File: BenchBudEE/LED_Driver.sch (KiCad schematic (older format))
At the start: 0 parts

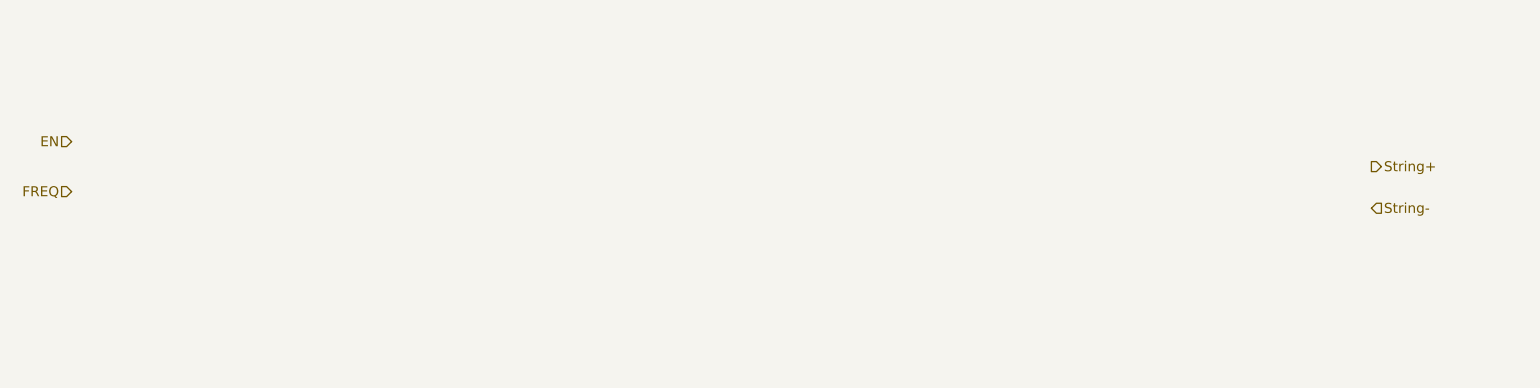
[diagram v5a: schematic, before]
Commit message: LED Driver module sketched out from AP5726 chip
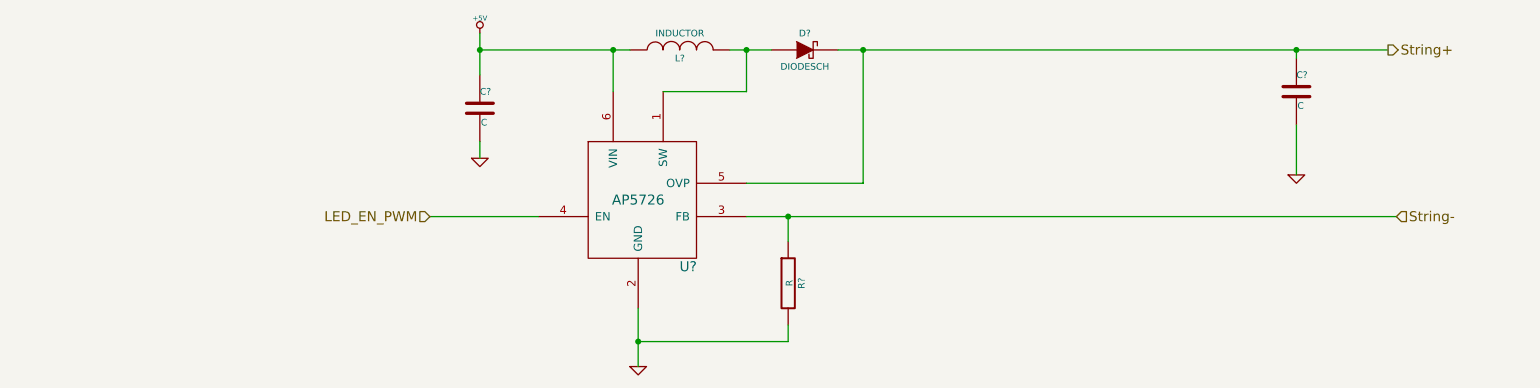
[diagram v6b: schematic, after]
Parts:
- added C? (x2): C, ~, symbol C
- added D?: DIODESCH, ~, symbol DIODESCH
- added L?: INDUCTOR, ~, symbol INDUCTOR
- added R?: R, ~, symbol R
- added U?: AP5726, symbol AP5726
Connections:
- net String+: now also C?.1, D?.2 (K), U?.5 (OVP)
- net String-: now also R?.1, U?.3 (FB)
- new net: D?.1 (A), L?.2, U?.1 (SW)
- new net +5V: C?.1, L?.1, U?.6 (VIN)
- new net GND: C?.2, C?.2, R?.2, U?.2 (GND)
- new net LED_EN_PWM: U?.4 (EN)
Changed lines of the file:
@@
 Comment4 ""
 $EndDescr
-Text HLabel 1600 2500 0    60   Input ~ 0
-EN
-Text HLabel 1600 2800 0    60   Input ~ 0
-FREQ
-Text HLabel 9400 2650 2    60   Output ~ 0
+Text HLabel 3750 2950 0    60   Input ~ 0
+LED_EN_PWM
+Text HLabel 9500 1950 2    60   Output ~ 0
 String+
-Text HLabel 9400 2900 2    60   Input ~ 0
+Text HLabel 9550 2950 2    60   Input ~ 0
 String-
+$Comp
+L AP5726 U?
+U 1 1 52F3F91E
+P 5000 2850
+F 0 "U?" H 5300 2450 60  0000 C CNN
+F 1 "AP5726" H 5000 2850 60  0000 C CNN
+F 2 "" H 4950 2900 60  0000 C CNN
+F 3 "" H 4950 2900 60  0000 C CNN
+	1    5000 2850
+	1    0    0    -1
+$EndComp
+$Comp
+L +5V #PWR?
+U 1 1 52F3FC4A
+P 4050 1850
+F 0 "#PWR?" H 4050 1940 20  0001 C CNN
+F 1 "+5V" H 4050 1940 30  0000 C CNN
+F 2 "" H 4050 1850 60  0000 C CNN
+F 3 "" H 4050 1850 60  0000 C CNN
+	1    4050 1850
+	1    0    0    -1
+$EndComp
+$Comp
+L GND #PWR?
+U 1 1 52F3FC59
+P 5000 3850
+F 0 "#PWR?" H 5000 3850 30  0001 C CNN
+F 1 "GND" H 5000 3780 30  0001 C CNN
+F 2 "" H 5000 3850 60  0000 C CNN
+F 3 "" H 5000 3850 60  0000 C CNN
+	1    5000 3850
+	1    0    0    -1
+$EndComp
+Wire Wire Line
+	5000 3500 5000 3850
+$Comp
+L GND #PWR?
+U 1 1 52F3FC67
+P 4050 2600
+F 0 "#PWR?" H 4050 2600 30  0001 C CNN
+F 1 "GND" H 4050 2530 30  0001 C CNN
+F 2 "" H 4050 2600 60  0000 C CNN
+F 3 "" H 4050 2600 60  0000 C CNN
+	1    4050 2600
+	1    0    0    -1
+$EndComp
+$Comp
+L C C?
+U 1 1 52F3FC6F
+P 4050 2300
+F 0 "C?" H 4050 2400 40  0000 L CNN
+F 1 "C" H 4056 2215 40  0000 L CNN
+F 2 "~" H 4088 2150 30  0000 C CNN
+F 3 "~" H 4050 2300 60  0000 C CNN
+	1    4050 2300
+	1    0    0    -1
+$EndComp
+Wire Wire Line
+	4050 1850 4050 2100
+Wire Wire Line
+	4050 2500 4050 2600
+Wire Wire Line
+	4050 1950 4950 1950
+Wire Wire Line
+	4850 1950 4850 2200
+Connection ~ 4050 1950
+$Comp
+L INDUCTOR L?
+U 1 1 52F3FC91
+P 5250 1950
+F 0 "L?" V 5200 1950 40  0000 C CNN
+F 1 "INDUCTOR" V 5350 1950 40  0000 C CNN
+F 2 "~" H 5250 1950 60  0000 C CNN
+F 3 "~" H 5250 1950 60  0000 C CNN
+	1    5250 1950
+	0    -1   -1   0
+$EndComp
+Connection ~ 4850 1950
+Wire Wire Line
+	5550 1950 5800 1950
+Wire Wire Line
+	5650 1950 5650 2200
+Wire Wire Line
+	5650 2200 5150 2200
+$Comp
+L DIODESCH D?
+U 1 1 52F3FCBF
+P 6000 1950
+F 0 "D?" H 6000 2050 40  0000 C CNN
+F 1 "DIODESCH" H 6000 1850 40  0000 C CNN
+F 2 "~" H 6000 1950 60  0000 C CNN
+F 3 "~" H 6000 1950 60  0000 C CNN
+	1    6000 1950
+	1    0    0    -1
+$EndComp
+Connection ~ 5650 1950
+Wire Wire Line
+	5650 2750 6350 2750
+Wire Wire Line
+	6350 2750 6350 1950
+Wire Wire Line
+	6200 1950 9500 1950
+$Comp
+L C C?
+U 1 1 52F3FCE4
+P 8950 2200
+F 0 "C?" H 8950 2300 40  0000 L CNN
+F 1 "C" H 8956 2115 40  0000 L CNN
+F 2 "~" H 8988 2050 30  0000 C CNN
+F 3 "~" H 8950 2200 60  0000 C CNN
+	1    8950 2200
+	1    0    0    -1
+$EndComp
+Wire Wire Line
+	8950 1950 8950 2000
+Connection ~ 6350 1950
+$Comp
+L GND #PWR?
+U 1 1 52F3FCF9
+P 8950 2700
+F 0 "#PWR?" H 8950 2700 30  0001 C CNN
+F 1 "GND" H 8950 2630 30  0001 C CNN
+F 2 "" H 8950 2700 60  0000 C CNN
+F 3 "" H 8950 2700 60  0000 C CNN
+	1    8950 2700
+	1    0    0    -1
+$EndComp
+Wire Wire Line
+	8950 2400 8950 2700
+Connection ~ 8950 1950
+Wire Wire Line
+	9550 2950 5650 2950
+$Comp
+L R R?
+U 1 1 52F3FD3D
+P 5900 3350
+F 0 "R?" V 5980 3350 40  0000 C CNN
+F 1 "R" V 5907 3351 40  0000 C CNN
+F 2 "~" V 5830 3350 30  0000 C CNN
+F 3 "~" H 5900 3350 30  0000 C CNN
+	1    5900 3350
+	1    0    0    -1
+$EndComp
+Wire Wire Line
+	5900 3600 5900 3700
+Wire Wire Line
+	5900 3700 5000 3700
+Connection ~ 5000 3700
+Wire Wire Line
+	5900 3100 5900 2950
+Connection ~ 5900 2950
+Wire Wire Line
+	3750 2950 4400 2950
 $EndSCHEMATC

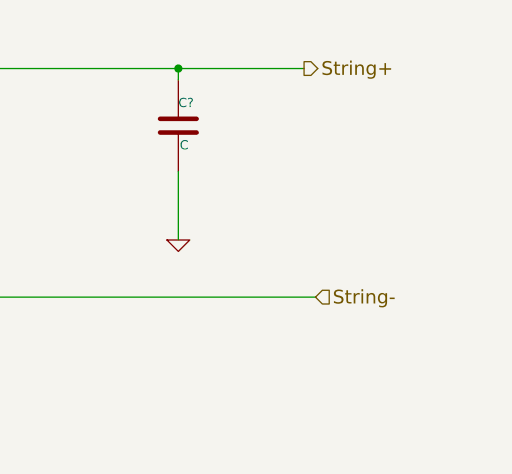
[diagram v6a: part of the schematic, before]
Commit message: Schematic modules connected together and to arduino pins
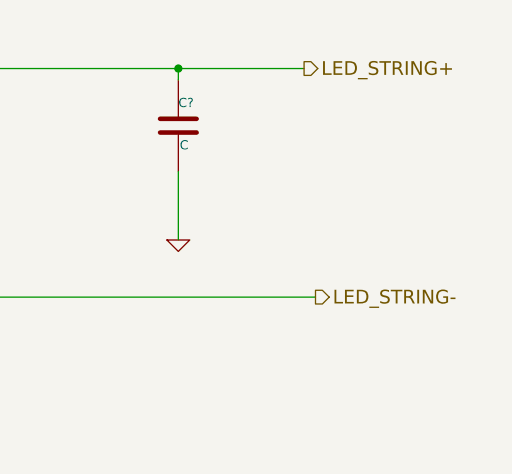
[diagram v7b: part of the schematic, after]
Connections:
- net String+ renamed LED_STRING+
- net String- renamed LED_STRING-
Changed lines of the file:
@@
 LIBS:valves
 LIBS:CE Library
+LIBS:atx_24pin_power
 LIBS:BenchBudEE-cache
 EELAYER 27 0
@@
 $Descr A4 11693 8268
 encoding utf-8
-Sheet 4 9
+Sheet 3 9
 Title ""
-Date "6 feb 2014"
+Date "8 feb 2014"
 Rev ""
 Comp ""
@@
 LED_EN_PWM
 Text HLabel 9500 1950 2    60   Output ~ 0
-String+
-Text HLabel 9550 2950 2    60   Input ~ 0
-String-
+LED_STRING+
+Text HLabel 9550 2950 2    60   Output ~ 0
+LED_STRING-
 $Comp
 L AP5726 U?
